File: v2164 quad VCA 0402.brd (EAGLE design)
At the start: 40 x 14.3 mm, 43 parts, among them IC1 TL072JD, IC2 TL072JD

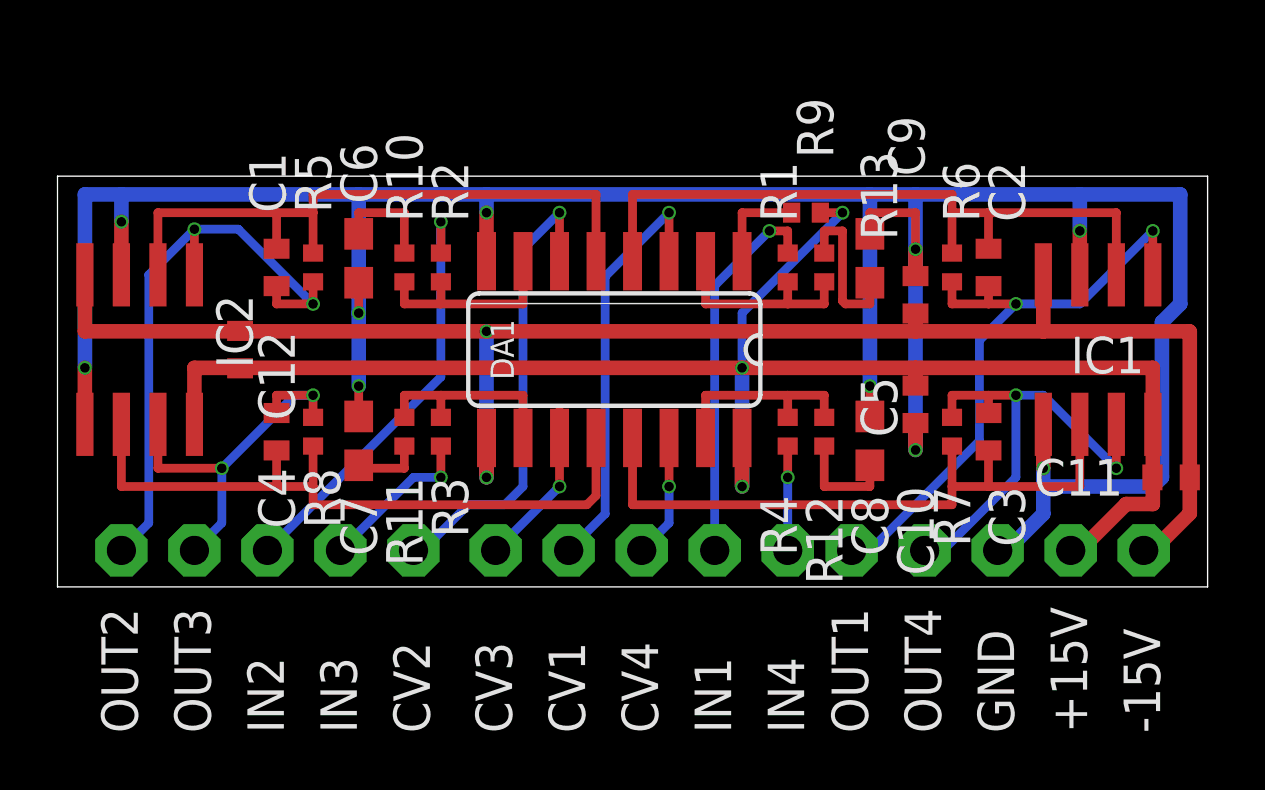
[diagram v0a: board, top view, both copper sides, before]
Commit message: Added ground plane
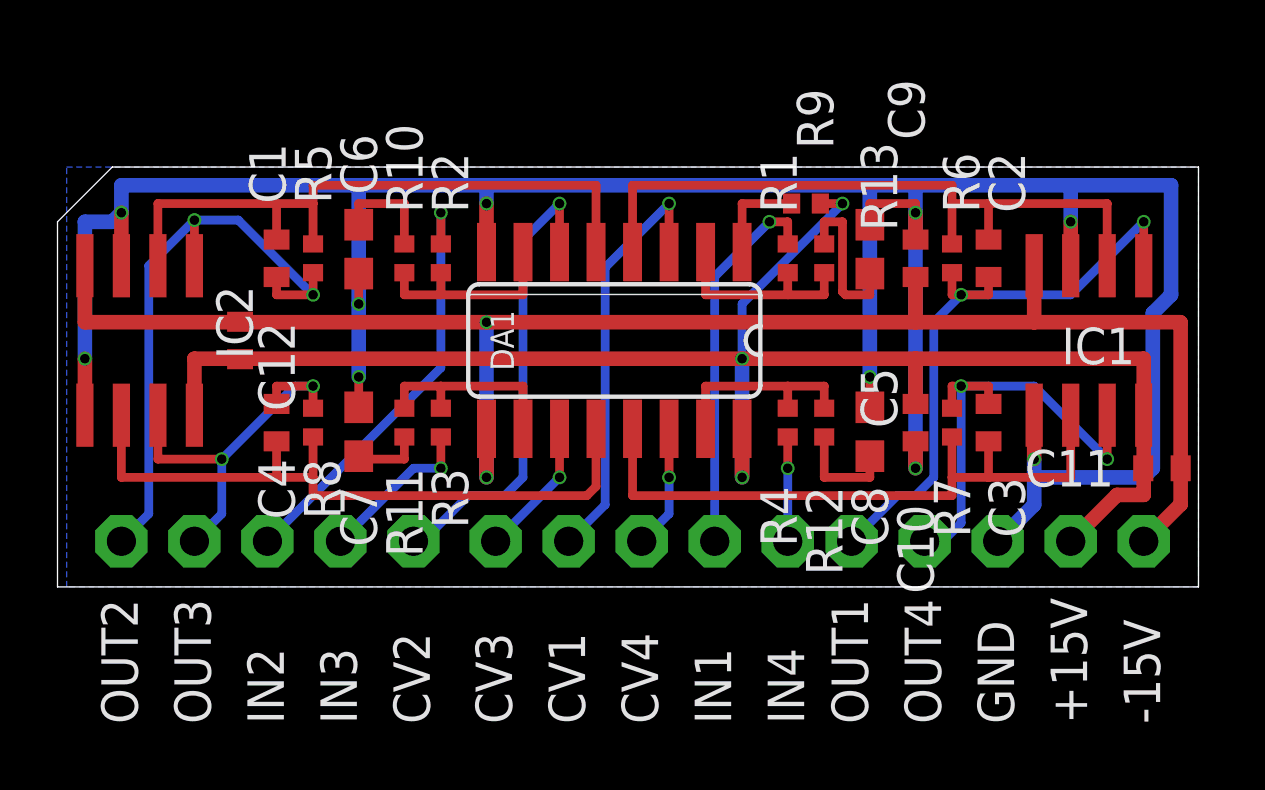
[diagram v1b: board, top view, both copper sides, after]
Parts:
- moved C9 1.27 mm to (29.8, 11.4)
- moved C10 0.63 mm to (29.8, 5.71)
- moved C11 0.45 mm to (38.4, 4.13)
- moved IC1 0.45 mm to (35.9, 8.57)
- moved C5 0.32 mm to (28.3, 11.7)
- moved C6 0.32 mm to (10.5, 11.7)
- moved R13 0.32 mm to (26.0, 13.3)
- moved +15V 0.32 mm to (35.2, 1.59)
- moved -15V 0.32 mm to (37.8, 1.59)
- moved C3 0.32 mm to (32.4, 5.71)
- moved C4 0.32 mm to (7.62, 5.71)
- moved C7 0.32 mm to (10.5, 5.40)
- moved C8 0.32 mm to (28.3, 5.40)
- moved CV1 0.32 mm to (17.8, 1.59)
- moved CV2 0.32 mm to (12.4, 1.59)
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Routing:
- net GND: track 104.5 -> 102.7 mm
- net -15V: track 57.9 -> 58.9 mm
- net CV3: track 5.78 -> 4.83 mm
- added copper zone on layer 16, net GND
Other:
- board size 40 x 14.3 mm -> 39.7 x 14.6 mm

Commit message: Added ground plane
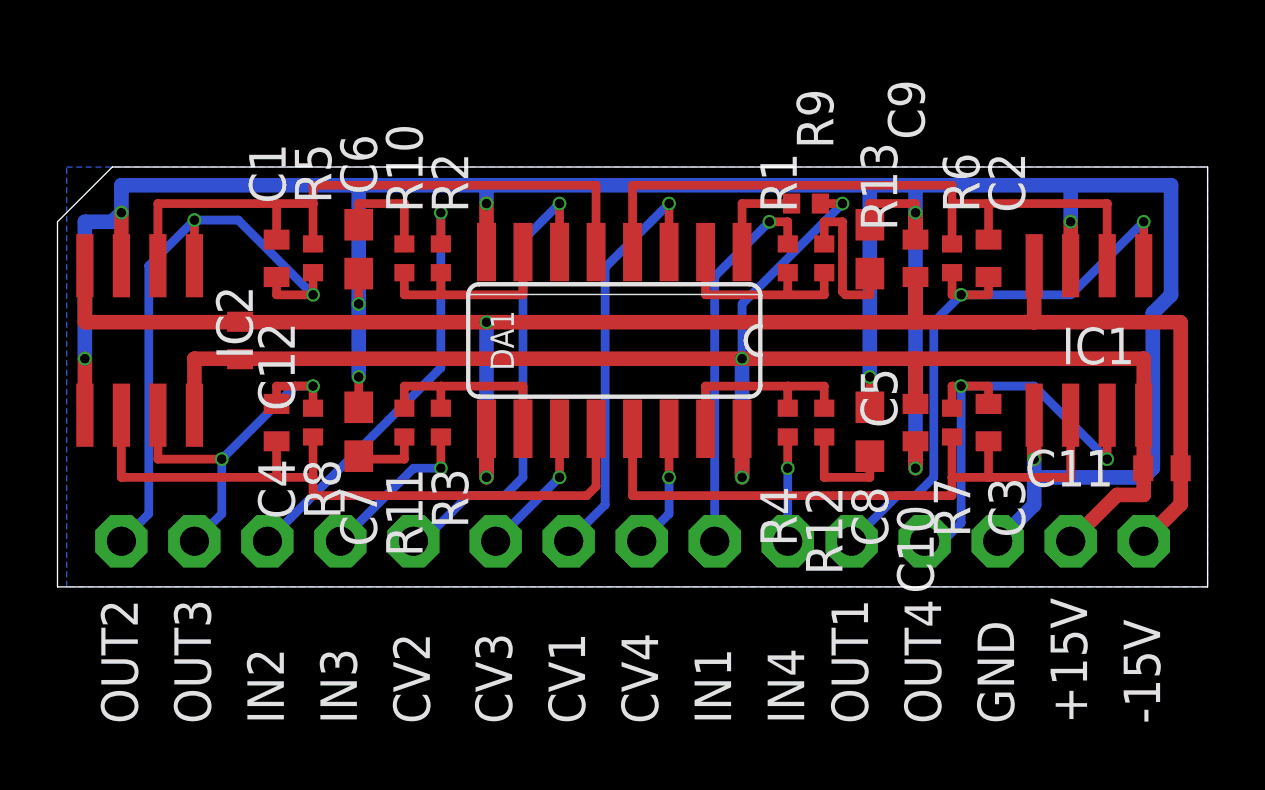
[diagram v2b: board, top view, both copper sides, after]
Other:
- board size 39.7 x 14.6 mm -> 40 x 14.6 mm
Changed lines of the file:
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@@
 <board>
 <plain>
-<wire x1="0" y1="0" x2="39.6875" y2="0" width="0" layer="20"/>
-<wire x1="39.6875" y1="0" x2="39.6875" y2="14.605" width="0" layer="20"/>
-<wire x1="39.6875" y1="14.605" x2="1.905" y2="14.605" width="0" layer="20"/>
+<wire x1="0" y1="0" x2="40.005" y2="0" width="0" layer="20"/>
+<wire x1="40.005" y1="0" x2="40.005" y2="14.605" width="0" layer="20"/>
+<wire x1="40.005" y1="14.605" x2="1.905" y2="14.605" width="0" layer="20"/>
 <wire x1="1.905" y1="14.605" x2="0" y2="12.7" width="0" layer="20"/>
 <wire x1="0" y1="12.7" x2="0" y2="0" width="0" layer="20"/>
@@
 <vertex x="0.3175" y="0"/>
 <vertex x="0.3175" y="14.605"/>
-<vertex x="39.6875" y="14.605"/>
-<vertex x="39.6875" y="0"/>
+<vertex x="40.005" y="14.605"/>
+<vertex x="40.005" y="0"/>
 </polygon>
 </signal>
